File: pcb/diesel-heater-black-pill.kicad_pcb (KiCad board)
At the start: 2 copper layers, 80 x 40 mm, 28 parts, among them J1 5V Power, J10 Motor, J11 Glow Plug, J12 Oil Plug, J2 Black Pill Left, J3 Black Pill Right, J4 Buttons, J5 Hall Sensor, J6 Battery Mon, J7 OLED, J8 NTC50K Room Temperature, J9 NTC50K Outlet Temperature

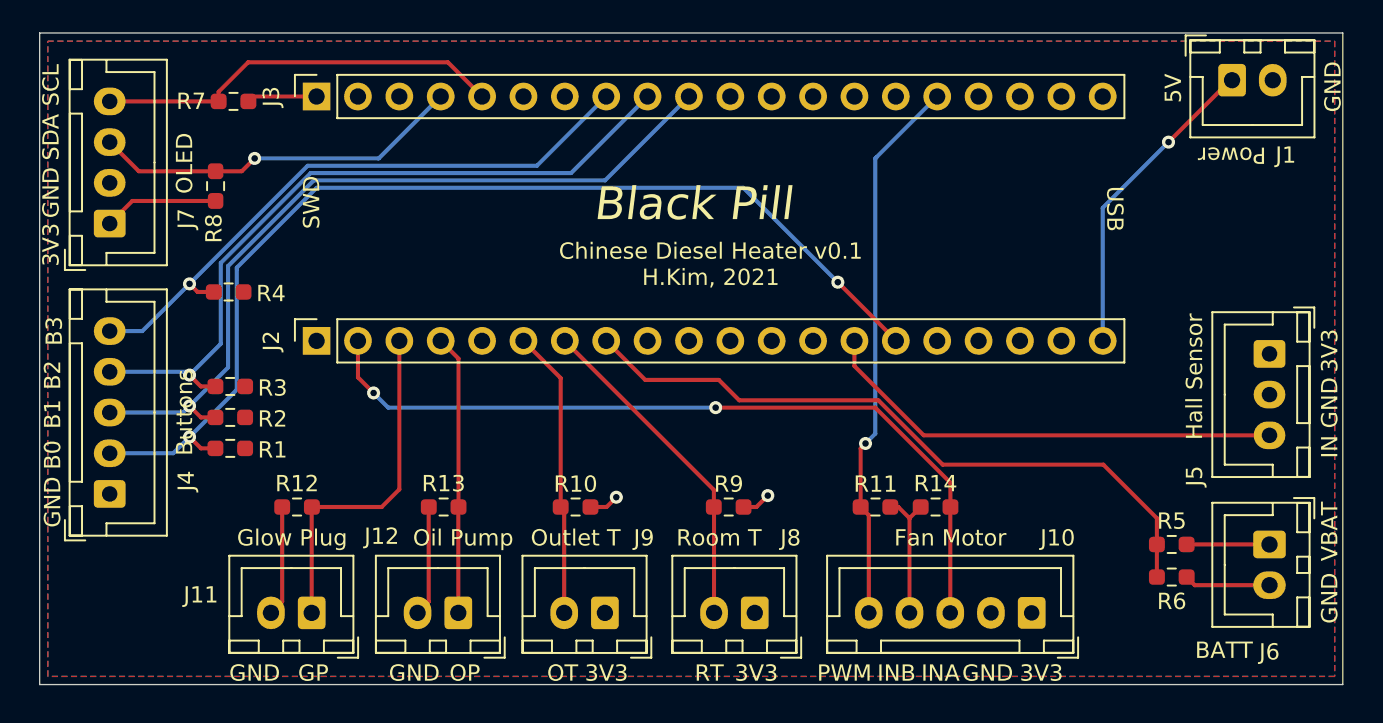
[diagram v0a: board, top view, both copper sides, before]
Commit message: changed pcb to add esp-01
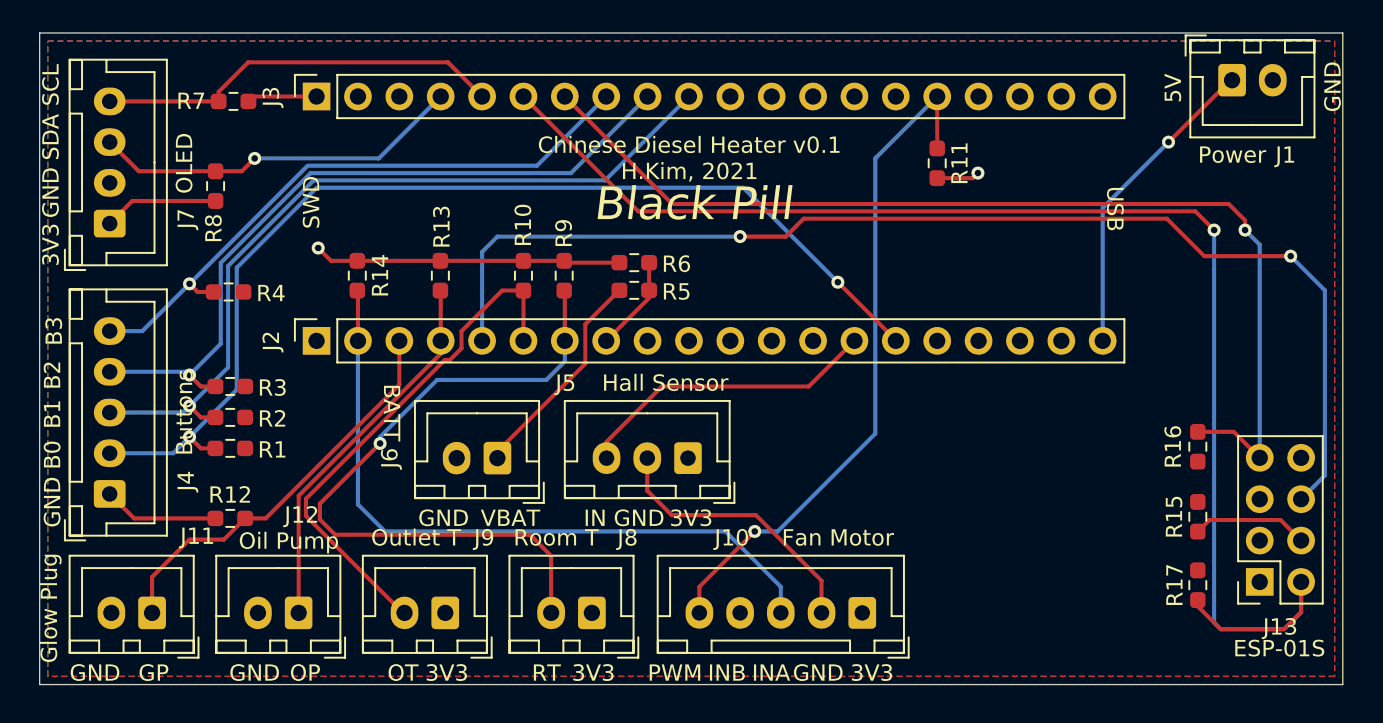
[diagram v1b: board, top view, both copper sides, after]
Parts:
- added J13: ESP-01S, Connector_PinSocket_2.54mm:PinSocket_2x04_P2.54mm_Vertical, F.Cu at (154.9, 93.7)
- added R15: 2K, Resistor_SMD:R_0603_1608Metric_Pad0.98x0.95mm_HandSolder, F.Cu at (151.1, 89.7)
- added R16: 100K, Resistor_SMD:R_0603_1608Metric_Pad0.98x0.95mm_HandSolder, F.Cu at (151.1, 85.4)
- added R17: 100K, Resistor_SMD:R_0603_1608Metric_Pad0.98x0.95mm_HandSolder, F.Cu at (151.1, 93.9)
- moved J6 47.7 mm to (108.1, 86.1), turned to 180 degrees
- moved R14 38.2 mm to (99.5, 74.9), turned to 270 degrees
- moved R6 38.2 mm to (116.5, 74.1), turned to 180 degrees
- moved R5 36.5 mm to (116.5, 75.8), turned to 180 degrees
- moved J5 36.3 mm to (119.8, 86.1), turned to 180 degrees
- moved R11 21.4 mm to (135.1, 68.0), turned to 90 degrees
- moved R9 17.4 mm to (112.2, 74.9), turned to 270 degrees
- moved R10 14.6 mm to (109.7, 74.9), turned to 270 degrees
- moved R13 14.2 mm to (104.6, 74.9), turned to 270 degrees
- moved J10 10.4 mm to (130.5, 95.6)
- moved J8 10.0 mm to (113.9, 95.6)
- moved J11 9.80 mm to (86.9, 95.6)
- moved J12 9.80 mm to (95.9, 95.6)
- moved J9 9.80 mm to (104.9, 95.6)
- moved R12 4.16 mm to (91.7, 89.8)
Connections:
- J2 pad 5: Net-(J2-Pad5) -> /RST
- J3 pad 6: Net-(J3-Pad6) -> /W_TXD
- J3 pad 7: Net-(J3-Pad7) -> /W_RXD
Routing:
- net /W_TXD: track 0.00 -> 88.1 mm, vias 0 -> 1
- net /RST: track 0.00 -> 73.3 mm, vias 0 -> 2
- net /W_RXD: track 0.00 -> 64.8 mm, vias 0 -> 1
- net /VPWR: track 41.9 -> 5.89 mm
- net /RT: track 20.5 -> 43.4 mm, vias 0 -> 1
- net /OT: track 17.7 -> 31.9 mm
- net GND: track 31.4 -> 45.6 mm
- net /M_RUN: track 28.8 -> 18.8 mm
- net /VBAT: track 5.09 -> 13.4 mm
- net /M_PWM: track 33.9 -> 41.8 mm
- net /W_CH_PD: track 0.00 -> 7.16 mm
- net /M_INA: track 49.3 -> 42.8 mm, vias 2 -> 0
- net /OP_SIG: track 17.2 -> 23.4 mm
- net /GP_SIG: track 21.4 -> 25.0 mm
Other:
- board text added: "ESP-01S"

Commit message: minor pcb modification
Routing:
- net /3V3: track 11.4 -> 7.50 mm
- net /RST: track 73.3 -> 72.6 mm

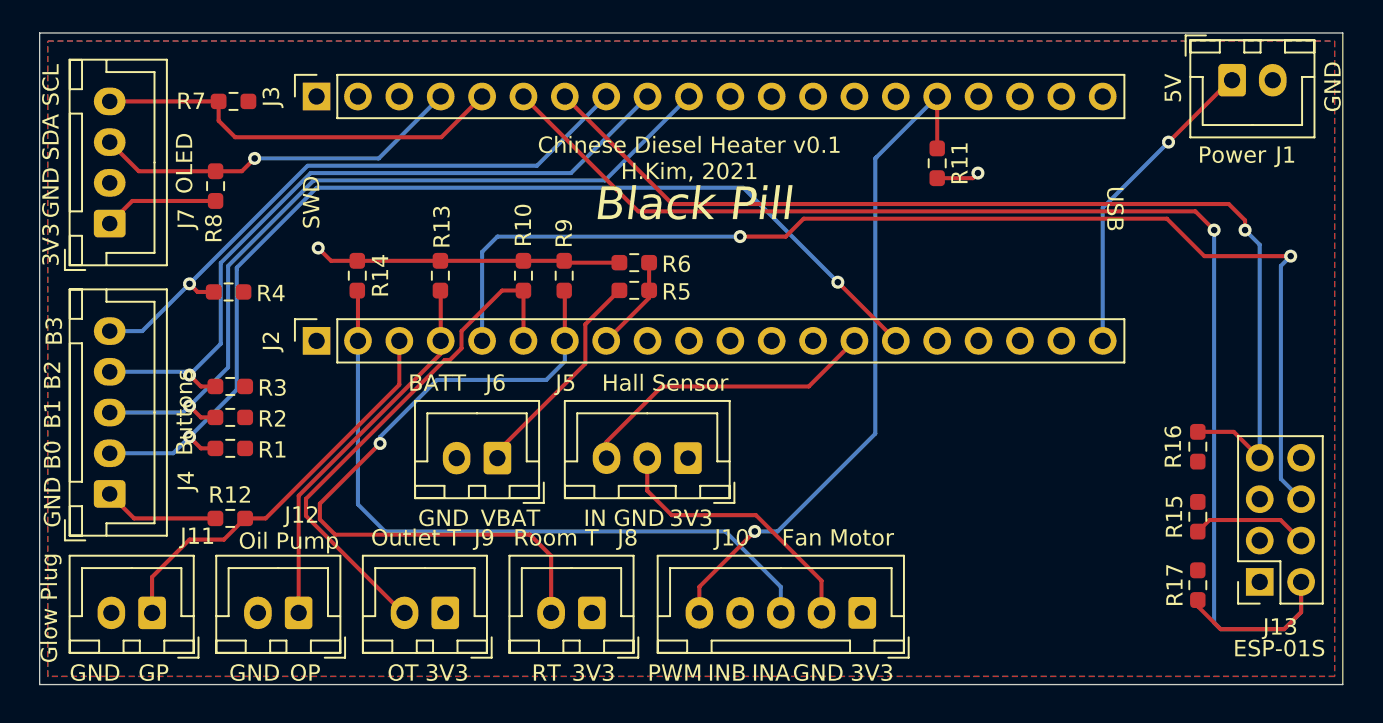
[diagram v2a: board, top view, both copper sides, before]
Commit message: changed dimension from 15mm to 15.24mm
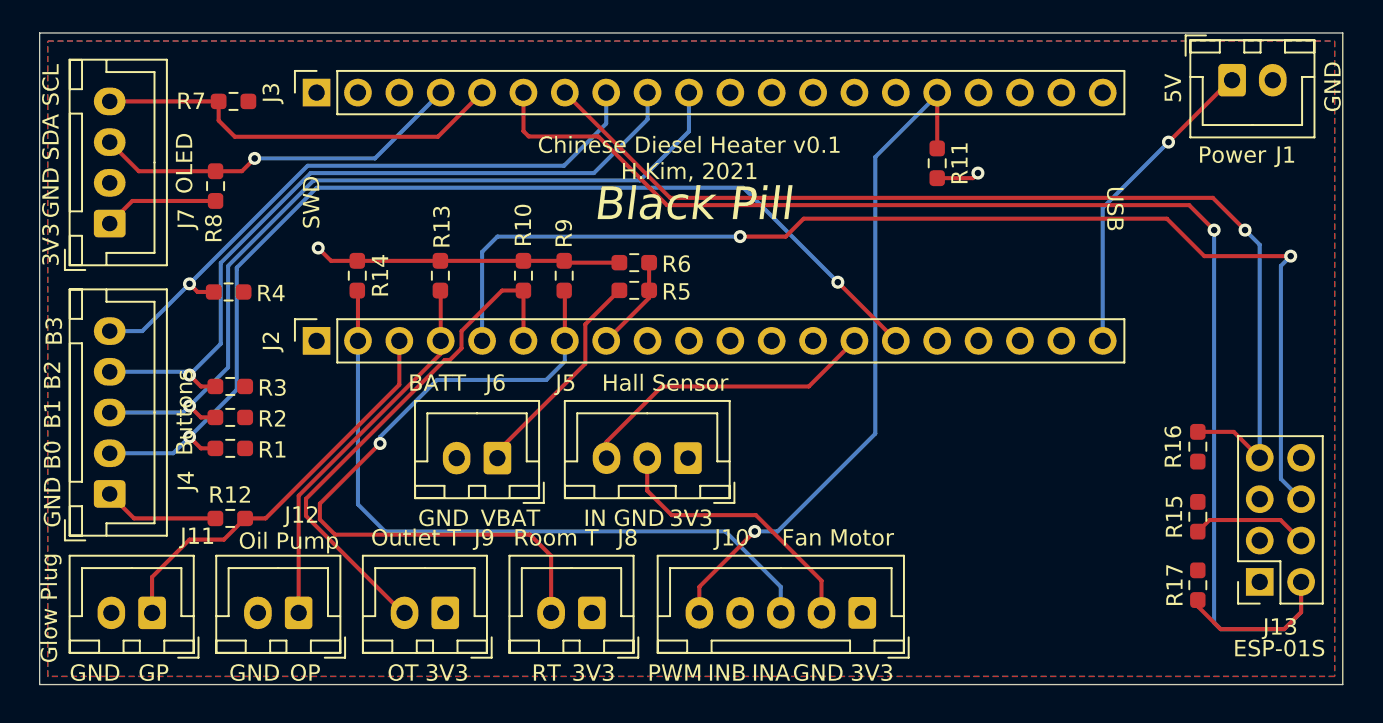
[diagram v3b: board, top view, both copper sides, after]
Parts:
- moved J3 0.24 mm to (97.0, 63.7)
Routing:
- net /BTN1: track 49.1 -> 50.6 mm
- net /W_TXD: track 88.1 -> 89.6 mm
- net /BTN3: track 38.1 -> 39.4 mm
- net /BTN2: track 45.0 -> 46.0 mm

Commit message: changed to use PB10 for motor INA
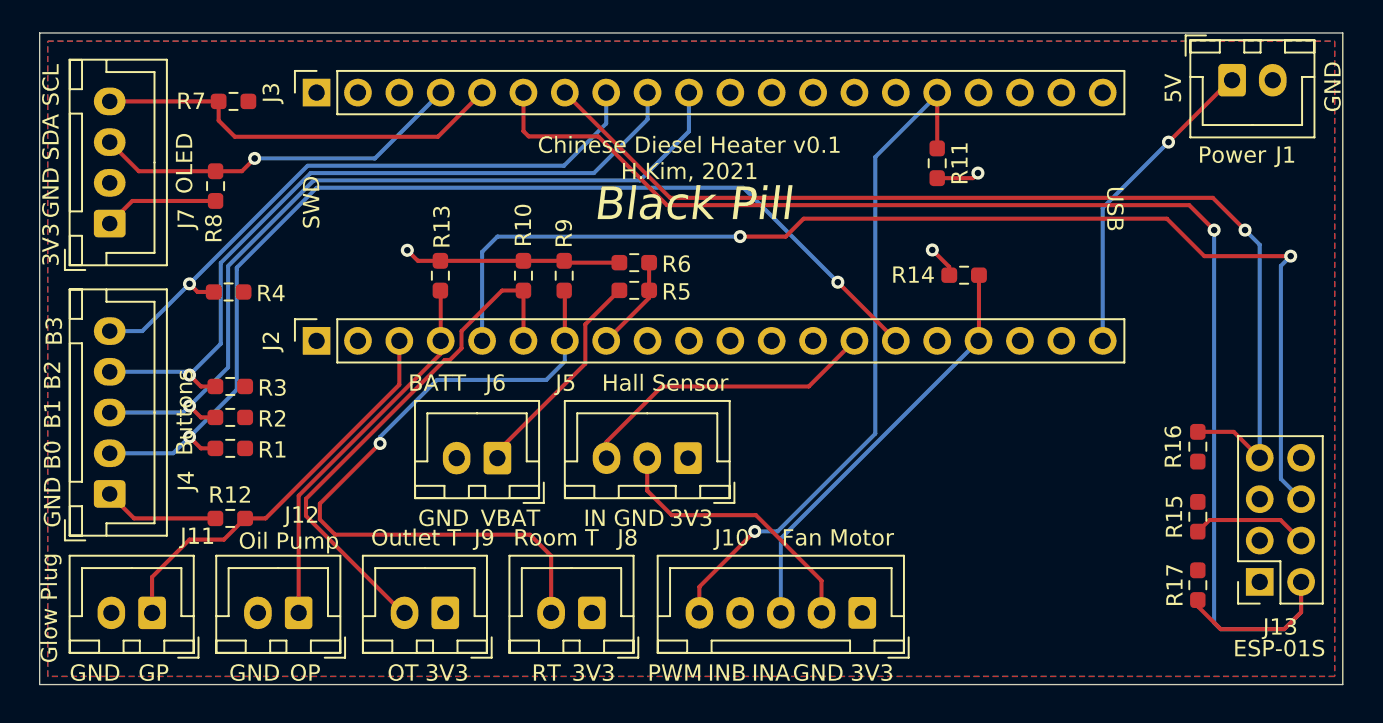
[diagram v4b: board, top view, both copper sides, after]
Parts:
- moved R14 37.3 mm to (136.8, 74.9), turned to 0 degrees
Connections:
- J2 pad 17: Net-(J2-Pad17) -> /M_INA
- J2 pad 2: /M_INA -> /LED
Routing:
- net /M_INA: track 42.8 -> 25.8 mm
- net GND: track 45.6 -> 42.0 mm, vias 2 -> 3

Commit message: changed main power batter voltage divider from 6.3K to 33K
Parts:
- R5: value 6.8K -> 33K

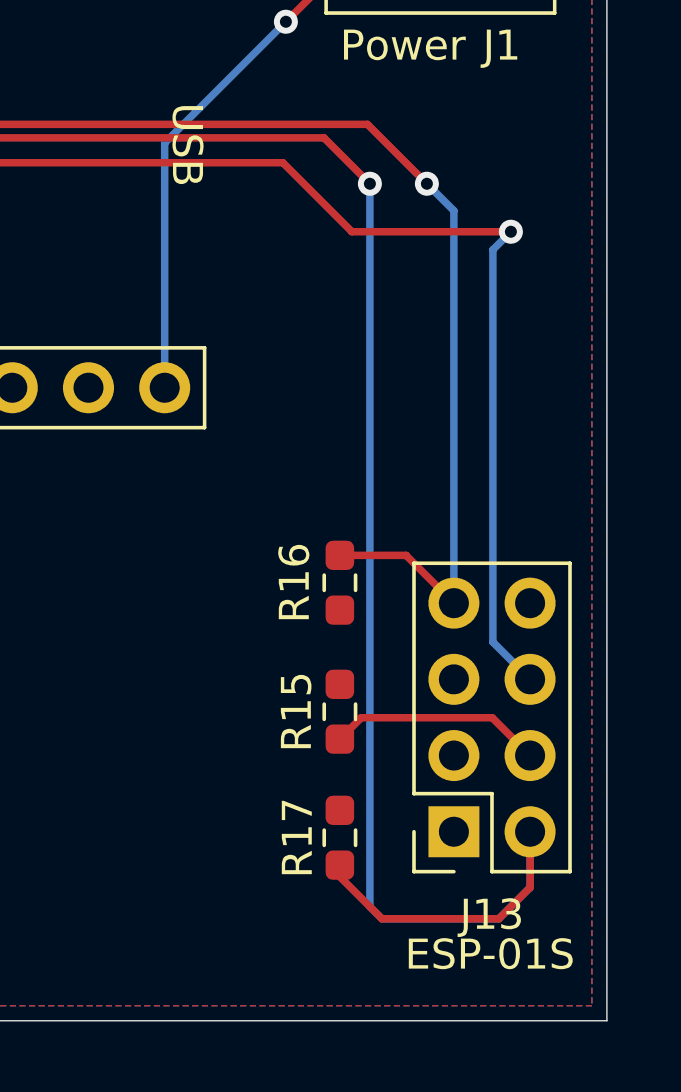
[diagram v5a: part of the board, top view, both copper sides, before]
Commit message: fixed unconnected pcb bug. kicad is weird after upgrading
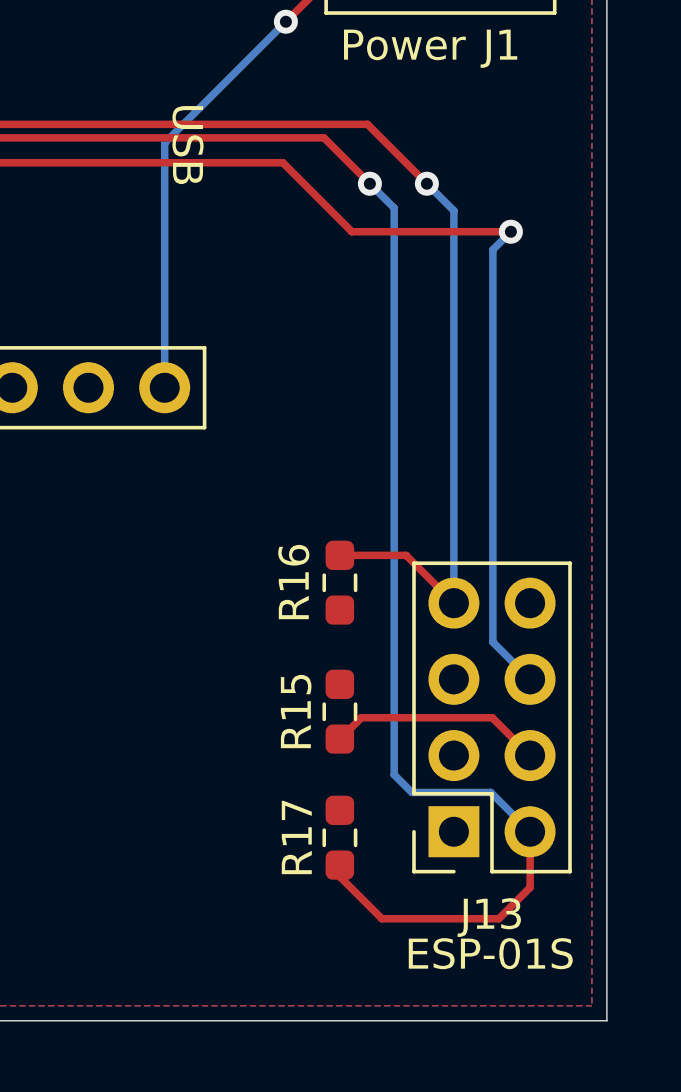
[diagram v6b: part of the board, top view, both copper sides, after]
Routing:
- net /W_TXD: track 89.6 -> 83.1 mm
